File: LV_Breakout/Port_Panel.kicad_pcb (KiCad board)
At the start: 2 copper layers, 24 parts, among them J1 DB9_Male_MountingHoles, J10 TE 776228-1, J2 B3B-PH-K-S(LF)(SN), J3 Conn_02x03_Odd_Even, J4 LD09S13A4GX00LF, J5 USB_B, J6 RJ45, J7 B6B-XH-A(LF)(SN), J8 B10B-PHDSS(LF)(SN), J9 RJ45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

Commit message: change port panel
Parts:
- moved J2 36.2 mm to (109.2, 76.7)
- moved J8 33.2 mm to (145.7, 76.2)
- moved J4 16.4 mm to (122.4, 95.0)
- moved J1 15.2 mm to (106.7, 106.0)
- moved J7 4.09 mm to (129.0, 76.7)
- moved U1 0.51 mm to (167.1, 69.8), turned to 90 degrees
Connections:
- J10 pad 1: /Sensor_1 -> (no net)
- J10 pad 10: /Sensor_10 -> /BMS_FAULT
- J10 pad 11: /CAN+ -> /CAN-
- J10 pad 13: /CAN- -> /Sensor_3
- J10 pad 14: /CAN- -> /Sensor_6
- J10 pad 15: /RINEHART_TX -> /Sensor_9
- J10 pad 16: /RINEHART_RX -> /RINEHART_TX
- J10 pad 17: /BMS_FAULT -> /RINEHART_RX
- J10 pad 18: (no net) -> /CAN-
- J10 pad 19: (no net) -> /CAN+
- J10 pad 2: /Sensor_2 -> GND
- J10 pad 20: GND -> /Sensor_1
- J10 pad 21: GND -> /Sensor_2
- J10 pad 22: GND -> /Sensor_5
- J10 pad 23: GND -> /Sensor_10
- J10 pad 3: /Sensor_3 -> GND
- J10 pad 4: /Sensor_4 -> GND
- J10 pad 5: /Sensor_5 -> GND
- J10 pad 6: /Sensor_6 -> /Sensor_4
- J10 pad 9: /Sensor_9 -> (no net)

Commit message: Updated PCB Layout
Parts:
- added G***: LOGO, AERO_CUSTOM:AERO_Logo_15x6mm, B.Cu at (164.5, 43.2)
- added Q1: PSMN5R2-60YL, Package_TO_SOT_SMD:LFPAK56, B.Cu at (148.0, 60.1)
- added R5: 100, Resistor_SMD:R_0603_1608Metric_Pad1.05x0.95mm_HandSolder, B.Cu at (144.1, 64.1)
- D1: moved to B.Cu
- J8: value B10B-PHDSS(LF)(SN) -> B12B-PUDSS-1(LF)(SN); footprint Connector_JST:JST_PHD_B10B-PHDSS_2x05_P2.00mm_Vertical -> Connector_JST:JST_PHD_B12B-PHDSS_2x06_P2.00mm_Vertical
- moved C3 12.6 mm to (166.8, 62.2), turned to 180 degrees
- moved J3 6.35 mm to (163.8, 55.2), turned to 0 degrees
- moved J8 2.86 mm to (142.9, 76.2)
- moved J7 2.67 mm to (126.4, 76.7)
- moved Y1 2.62 mm to (156.2, 81.3), turned to 180 degrees
- moved R2 2.54 mm to (160.0, 91.4)
- moved J2 1.81 mm to (107.4, 76.7)
- moved D1 1.75 mm to (151.4, 81.3)
- moved R3 1.51 mm to (167.4, 77.5)
- moved J10 1.42 mm to (128.3, 54.6)
- moved J1 1.27 mm to (105.4, 106.0)
- moved C1 0.65 mm to (170.4, 60.3)
- moved R1 0.40 mm to (167.4, 80.0)
- moved C5 0.16 mm to (169.9, 95.2)
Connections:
- J1 pad 0: Net-(J1-Pad0) -> GND
- J10 pad 1: (no net) -> /RINEHART_TX
- J10 pad 10: /BMS_FAULT -> /EMUS_Curr3
- J10 pad 11: /CAN- -> /CAN+
- J10 pad 12: /CAN+ -> /CAN-
- J10 pad 15: /Sensor_9 -> /Sensor_2
- J10 pad 16: /RINEHART_TX -> /EMUS_Curr1
- J10 pad 17: /RINEHART_RX -> /EMUS_Curr2
- J10 pad 18: /CAN- -> /BMS_FAULT
- J10 pad 20: /Sensor_1 -> /CAN-
- J10 pad 21: /Sensor_2 -> /Sensor_1
- J10 pad 23: /Sensor_10 -> /FAN_OUT
- J10 pad 9: (no net) -> /RINEHART_RX
- J8 pad 1: (no net) -> /BMS_USB+
- J8 pad 10: (no net) -> +12V
- J8 pad 2: /BMS_USB+ -> /BMS_USB-
- J8 pad 3: /BMS_USB- -> /CAN-
- J8 pad 4: /BMS_FAULT -> GND
- J8 pad 6: /BMS_USB_5V -> GND
- J8 pad 7: /CAN- -> /BMS_FAULT
- J8 pad 8: GND -> /BMS_USB_5V
- J8 pad 9: +12V -> /EMUS_Curr3
- U1 pad 24: /Sensor_9 -> (no net)
- U1 pad 25: /Sensor_10 -> /FAN_SIG
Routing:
- net +5V: track 0.00 -> 143.3 mm, vias 0 -> 4
- net /CAN+: track 0.00 -> 72.2 mm
- net /CAN-: track 0.00 -> 71.6 mm
- net /MISO: track 0.00 -> 65.2 mm, vias 0 -> 2
- net /MOSI: track 0.00 -> 62.8 mm, vias 0 -> 2
- net /RINEHART_RX: track 0.00 -> 61.9 mm
- net /RINEHART_TX: track 0.00 -> 61.9 mm
- net /SCK: track 0.00 -> 60.5 mm, vias 0 -> 2
- net /SCL: track 0.00 -> 57.2 mm, vias 0 -> 3
- net /SDA: track 0.00 -> 56.0 mm, vias 0 -> 3
- net /Sensor_4: track 0.00 -> 51.3 mm, vias 0 -> 1
- net /Sensor_3: track 0.00 -> 48.9 mm, vias 0 -> 1
- net /Sensor_6: track 0.00 -> 44.6 mm, vias 0 -> 2
- net /Sensor_7: track 0.00 -> 42.1 mm, vias 0 -> 2
- net /Sensor_5: track 0.00 -> 40.8 mm, vias 0 -> 1
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- added copper zone on B.Cu, net GND
- added copper zone on F.Cu, net GND
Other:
- net class Default: trace_width 0.25 -> 0.254
- net class POWER added: clearance 0.3, trace_width 0.6125, via_dia 1.2, via_drill 0.6
- board text added: "Port Pass Through G.Spearing 20.0228"

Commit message: Minor Layout Changes
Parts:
- removed G***: LOGO, AERO_CUSTOM:AERO_Logo_15x6mm
- added C10: 1u, Capacitor_SMD:C_0603_1608Metric_Pad1.05x0.95mm_HandSolder, B.Cu at (103.6, 68.9)
- added C6: 1u, Capacitor_SMD:C_0603_1608Metric_Pad1.05x0.95mm_HandSolder, B.Cu at (118.4, 63.6)
- added C7: 1u, Capacitor_SMD:C_0603_1608Metric_Pad1.05x0.95mm_HandSolder, B.Cu at (103.6, 65.7)
- added C8: 1u, Capacitor_SMD:C_0603_1608Metric_Pad1.05x0.95mm_HandSolder, B.Cu at (107.8, 61.0)
- added C9: 1u, Capacitor_SMD:C_0603_1608Metric_Pad1.05x0.95mm_HandSolder, B.Cu at (111.3, 61.0)
- added J11: 2.54mmPins, Connector_PinHeader_2.54mm:PinHeader_1x03_P2.54mm_Vertical, B.Cu at (146.8, 82.3)
- added U4: MAX232, Package_SO:SOIC-16_3.9x9.9mm_P1.27mm, B.Cu at (111.3, 67.1)
- J1: value DB9_Male_MountingHoles -> 171-009-113R001
- J4: value LD09S13A4GX00LF -> 171-009-213R001
- moved D1 14.0 mm to (137.7, 83.8), turned to 90 degrees
- moved J6 12.7 mm to (145.8, 103.1), turned to 270 degrees
- moved J2 5.65 mm to (102.6, 79.7), turned to 90 degrees
- moved R4 1.82 mm to (169.8, 84.3)
- moved J9 0.46 mm to (159.0, 103.1)
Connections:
- J1 pad 2: (no net) -> /IMU_RX
- J1 pad 3: (no net) -> /IMU_TX
- J1 pad 5: (no net) -> GND
- J1 pad 9: (no net) -> +12V
- J2 pad 1: (no net) -> /IMU_TX_U
- J2 pad 2: (no net) -> /IMU_RX_U
- J6 pad 1: Net-(J6-Pad1) -> /E1_P
- J6 pad 2: Net-(J6-Pad2) -> /E1_N
- J6 pad 3: Net-(J6-Pad3) -> /E3_P
- J6 pad 4: Net-(J6-Pad4) -> /E2_P
- J6 pad 5: Net-(J6-Pad5) -> /E2_N
- J6 pad 6: Net-(J6-Pad6) -> /E3_N
- J6 pad 7: Net-(J6-Pad7) -> /E4_P
- J6 pad 8: Net-(J6-Pad8) -> /E4_N
- J8 pad 1: /BMS_USB+ -> GND
- J8 pad 2: /BMS_USB- -> GND
- J8 pad 4: GND -> /BMS_USB_5V
- J8 pad 6: GND -> /BMS_USB-
- J8 pad 8: /BMS_USB_5V -> /BMS_USB+
- J9 pad 1: Net-(J6-Pad8) -> /E1_P
- J9 pad 2: Net-(J6-Pad7) -> /E1_N
- J9 pad 3: Net-(J6-Pad6) -> /E3_P
- J9 pad 4: Net-(J6-Pad5) -> /E2_P
- J9 pad 5: Net-(J6-Pad4) -> /E2_N
- J9 pad 6: Net-(J6-Pad3) -> /E3_N
- J9 pad 7: Net-(J6-Pad2) -> /E4_P
- J9 pad 8: Net-(J6-Pad1) -> /E4_N
- U1 pad 30: (no net) -> /RXD
- U1 pad 31: (no net) -> /TXD
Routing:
- net /IMU_RX: track 0.00 -> 38.3 mm, vias 0 -> 1
- net /IMU_TX: track 0.00 -> 35.0 mm, vias 0 -> 1
- net Net-(J6-Pad7): track 30.0 -> 0.00 mm
- net Net-(J6-Pad3): track 30.0 -> 0.00 mm
- net Net-(J6-Pad1): track 30.0 -> 0.00 mm
- net Net-(J6-Pad5): track 30.0 -> 0.00 mm
- net Net-(J6-Pad6): track 30.0 -> 0.00 mm
- net Net-(J6-Pad4): track 30.0 -> 0.00 mm
- net Net-(J6-Pad8): track 30.0 -> 0.00 mm
- net Net-(J6-Pad2): track 30.0 -> 0.00 mm
- net +5V: track 143.3 -> 169.4 mm
- net +12V: track 19.4 -> 45.4 mm
- net /RXD: track 0.00 -> 21.9 mm
- net /BMS_USB-: track 33.1 -> 13.4 mm
- net /TXD: track 0.00 -> 19.3 mm
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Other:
- net class CAN added: clearance 0.2, trace_width 0.6, via_dia 0.8, via_drill 0.4
- net class ENet added: clearance 0.2, trace_width 0.254, via_dia 0.8, via_drill 0.4
- net class POWER: trace_width 0.6125 -> 1
- net class USB added: clearance 0.2, trace_width 0.57, via_dia 0.8, via_drill 0.4
- board text added: "BMS CONTROL"
- board text added: "FROM LVPDU"
- board text added: "GND"
- board text added: "IMU_IN"
- board text added: "IMU_UART"
- board text added: "RINEHART_OUT"
- board text added: "RXD"
- board text added: "TXD"

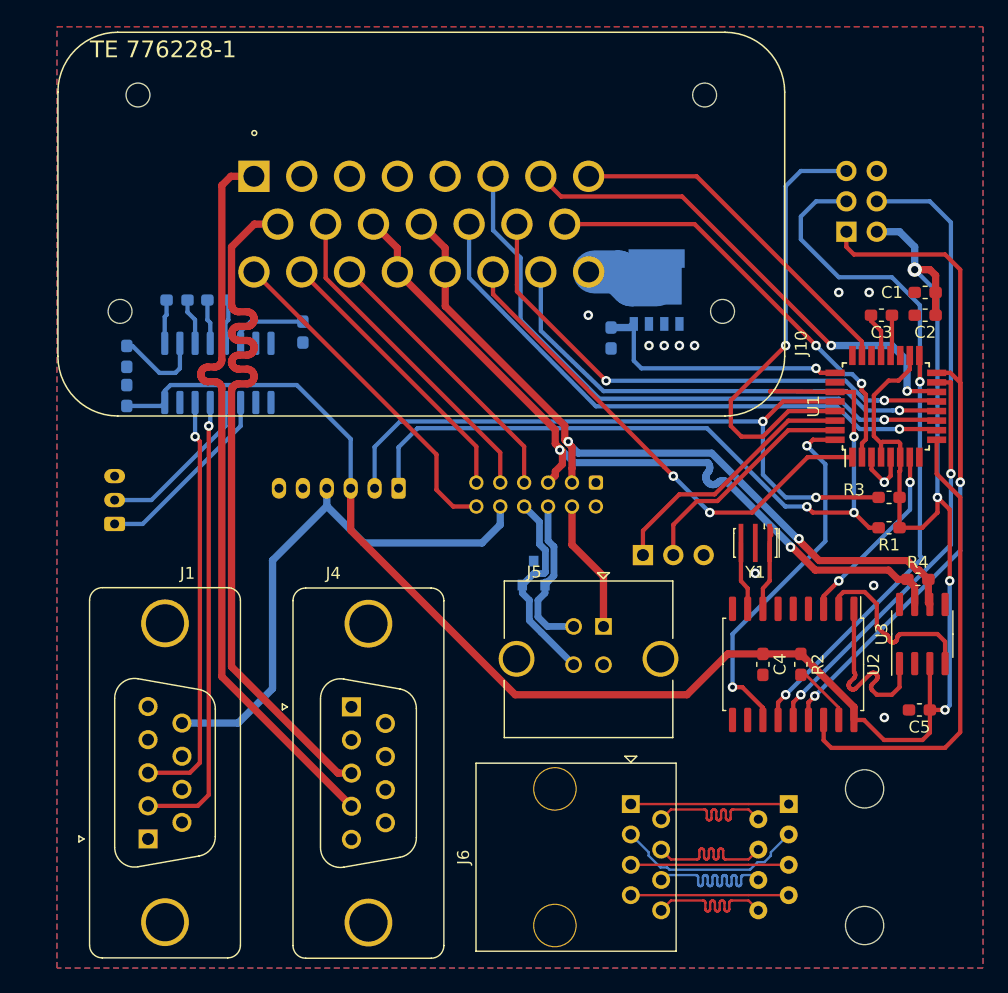
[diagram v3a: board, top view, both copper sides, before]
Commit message: Change trace and create Gerber
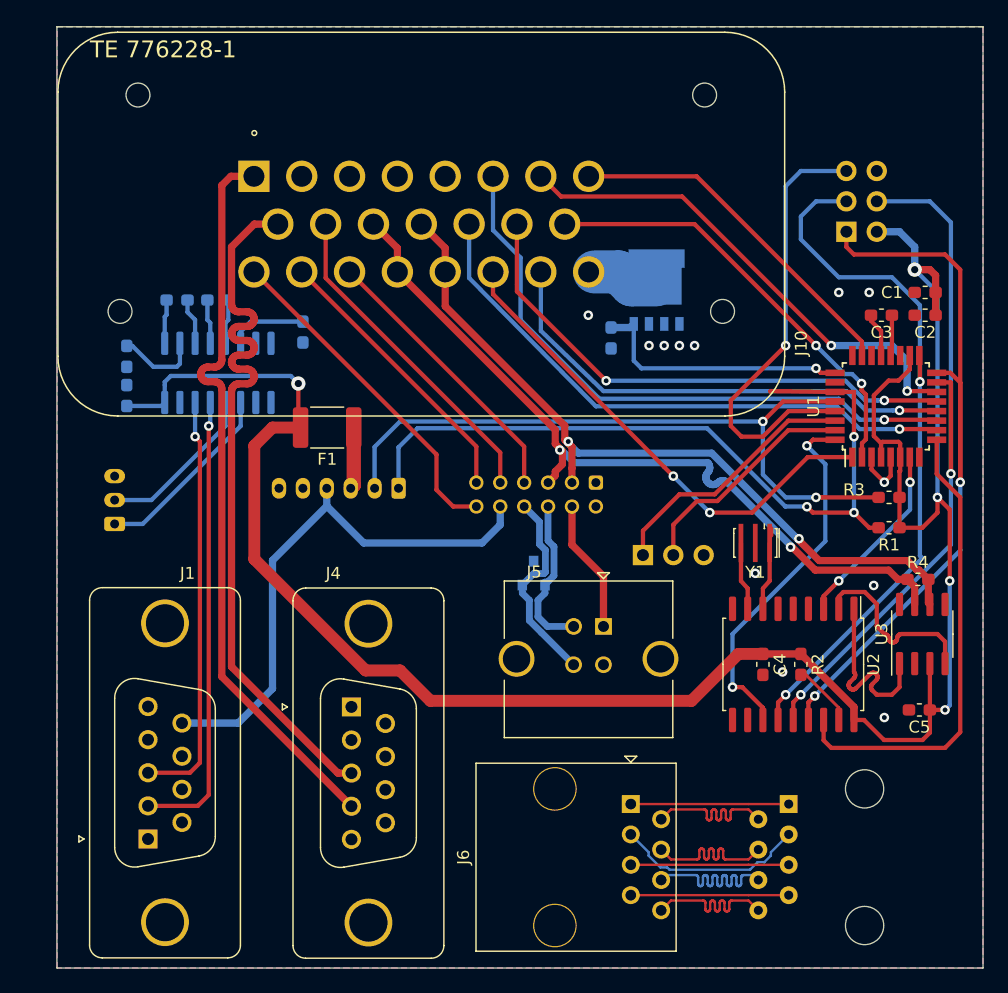
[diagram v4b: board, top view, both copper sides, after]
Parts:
- added F1: 1812L075/24, Fuse:Fuse_1812_4532Metric_Pad1.30x3.40mm_HandSolder, F.Cu at (120.4, 71.6)
- added G***: LOGO, AERO_CUSTOM:AERO_Logo_15x6mm, B.Cu at (165.1, 43.2)
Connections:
- J7 pad 3: +5V -> Net-(F1-Pad1)
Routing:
- net +5V: track 169.4 -> 181.7 mm, vias 4 -> 5
- net Net-(F1-Pad1): track 0.00 -> 5.19 mm
- net Net-(C7-Pad1): track 7.63 -> 6.99 mm
- net GND: vias 11 -> 12
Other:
- board outline added: 77.5 x 78.7 mm

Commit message: Minor changes / updates
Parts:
- removed G***: LOGO, AERO_CUSTOM:AERO_Logo_15x6mm
- added Q2: PSMN5R2-60YL, Package_TO_SOT_SMD:LFPAK56, B.Cu at (154.3, 49.5)
- added R6: 100, Resistor_SMD:R_0603_1608Metric_Pad1.05x0.95mm_HandSolder, F.Cu at (160.7, 59.7)
- J1: value 171-009-113R001 -> 171-009-113R911
- J10: footprint AERO_CUSTOM:TE_1-776200-1_23pin_Vertical -> AERO_FOOT:TE_1-776228-1_23P_VERT
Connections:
- J1 pad 6: (no net) -> +12V
- J10 pad 8: /Sensor_8 -> /BRAKE_OUT
- U1 pad 23: /Sensor_8 -> /BRAKE_SIG
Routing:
- net /Sensor_8: track 29.8 -> 0.00 mm
- net /BRAKE_SIG: track 0.00 -> 19.6 mm, vias 0 -> 1
- net +12V: track 45.4 -> 61.4 mm
- net /BRAKE_OUT: track 0.00 -> 12.7 mm
- net GND: vias 12 -> 14

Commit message: Create port panel model with connectors
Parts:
- F1: footprint Fuse:Fuse_1812_4532Metric_Pad1.30x3.40mm_HandSolder -> AERO_FOOT:Fuse_1812_4532Metric_Pad1.30x3.40mm_HandSolder
- J1: footprint Connector_Dsub:DSUB-9_Male_Vertical_P2.77x2.84mm_MountingHoles -> AERO_FOOT:DSUB-9_Male_TALL_DE09-PE-1-BL-JS
- J10: footprint AERO_FOOT:TE_1-776228-1_23P_VERT -> AERO_FOOT:TE_1-776228-1_23P_VERT_ASM
- J4: footprint Connector_Dsub:DSUB-9_Female_Vertical_P2.77x2.84mm_MountingHoles -> AERO_FOOT:DSUB-9_Female_TALL_DE09-SE-1-BL-JS
- J5: footprint Connector_USB:USB_B_TE_5787834_Vertical -> AERO_FOOT:USB_B_TE_5787834_Vertical
- J6: footprint Connector_RJ:RJ45_OST_PJ012-8P8CX_Vertical -> AERO_FOOT:RJ45_OST_PJ012-8P8CX_Vertical
- J8: footprint Connector_JST:JST_PHD_B12B-PHDSS_2x06_P2.00mm_Vertical -> AERO_FOOT:JST_PHD_B12B-PHDSS_2x06_P2.00mm_Vertical
- J9: footprint Connector_RJ:RJ45_Amphenol_54602-x08_Horizontal -> AERO_FOOT:RJ45_Amphenol_54602-x08_Horizontal
- Y1: footprint Crystal:Resonator_SMD_muRata_CSTxExxV-3Pin_3.0x1.1mm_HandSoldering -> AERO_FOOT:Resonator_SMD_muRata_CSTxExxV-3Pin_3.0x1.1mm_HandSoldering
